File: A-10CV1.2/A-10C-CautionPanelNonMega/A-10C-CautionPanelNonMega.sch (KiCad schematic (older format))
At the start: 29 parts, among them J1 Barrel_Jack, J10 Conn_01x24, J11 Conn_01x24, J13 Conn_01x03, J2 Nano Pins 1-15, J3 Nano Pins 16-30 (reversed), J4 Serial Tx/Rx, J8 Conn_01x24, J9 Conn_01x24, Q1 BC338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

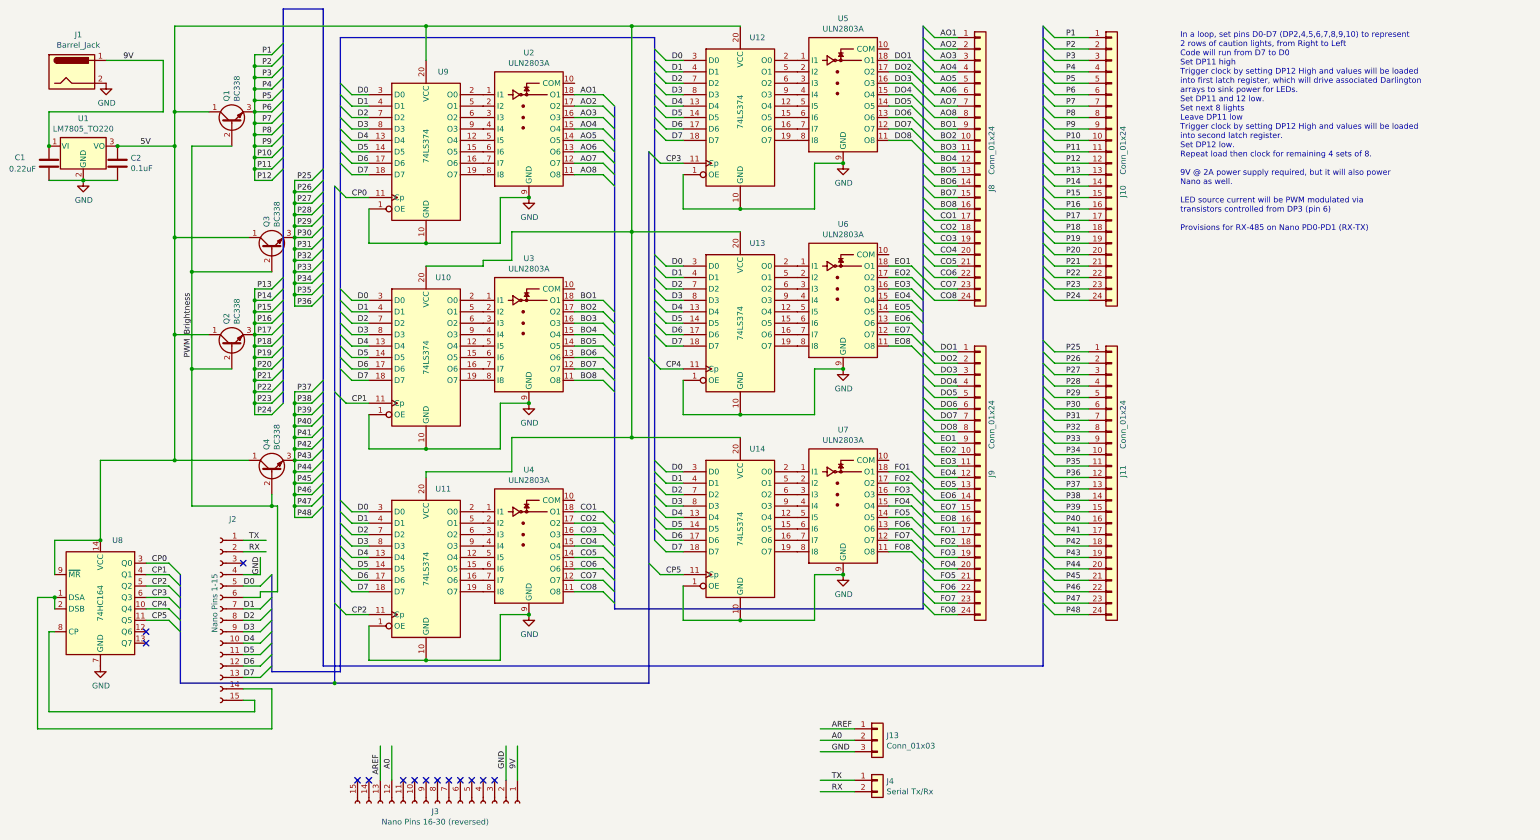
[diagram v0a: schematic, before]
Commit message: First bits of working code completed. May be changed in favor of single event vs 48 events.
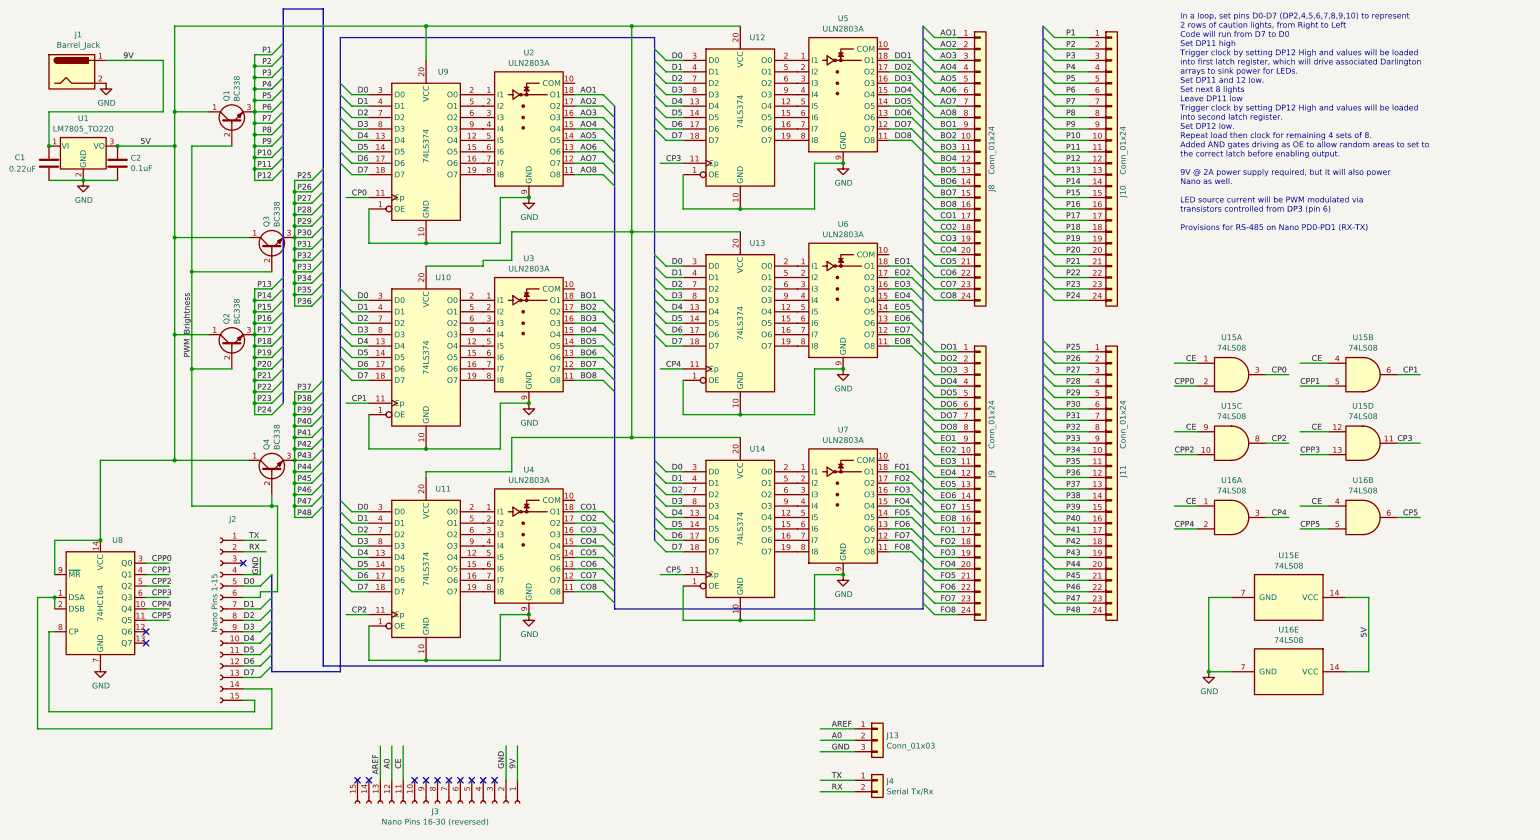
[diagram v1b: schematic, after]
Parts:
- added U15, U16: 74LS08, Package_DIP:DIP-14_W7.62mm, symbol 74xx:74LS08
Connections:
- net labels added: CE, CPP0, CPP1, CPP2, CPP3, CPP4, CPP5
- wire segments 408 -> 433
- no-connect marks 14 -> 13
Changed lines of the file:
@@
 NoConn ~ 1700 6050
 NoConn ~ 1700 6150
-Entry Wire Line
-	1900 5450 2000 5550
-Entry Wire Line
-	1900 5550 2000 5650
-Entry Wire Line
-	1900 5650 2000 5750
-Entry Wire Line
-	1900 5750 2000 5850
-Entry Wire Line
-	1900 5850 2000 5950
-Entry Wire Line
-	1900 5950 2000 6050
 Text Label 1750 5450 0    50   ~ 0
-CP0
+CPP0
 Text Label 1750 5550 0    50   ~ 0
-CP1
+CPP1
 Text Label 1750 5650 0    50   ~ 0
-CP2
+CPP2
 Text Label 1750 5750 0    50   ~ 0
-CP3
+CPP3
 Text Label 1750 5850 0    50   ~ 0
-CP4
+CPP4
 Text Label 1750 5950 0    50   ~ 0
-CP5
+CPP5
 Wire Wire Line
 	3650 5900 3450 5900
-Entry Wire Line
-	3350 5800 3450 5900
 Text Label 3500 5900 0    50   ~ 0
 CP2
 Wire Wire Line
 	3650 2250 3450 2250
-Entry Wire Line
-	3350 2150 3450 2250
 Text Label 3500 2250 0    50   ~ 0
 CP0
 Wire Wire Line
 	3650 4050 3450 4050
-Entry Wire Line
-	3350 3950 3450 4050
 Text Label 3500 4050 0    50   ~ 0
 CP1
 Wire Wire Line
 	6400 1950 6200 1950
-Entry Wire Line
-	6100 1850 6200 1950
 Text Label 6250 1950 0    50   ~ 0
 CP3
 Wire Wire Line
 	6400 3750 6200 3750
-Entry Wire Line
-	6100 3650 6200 3750
 Text Label 6250 3750 0    50   ~ 0
 CP4
 Wire Wire Line
 	6400 5550 6200 5550
-Entry Wire Line
-	6100 5450 6200 5550
 Text Label 6250 5550 0    50   ~ 0
 CP5
-Wire Bus Line
-	2000 6500 3350 6500
-Wire Bus Line
-	3350 6500 6100 6500
-Connection ~ 3350 6500
 Wire Wire Line
 	6400 5650 6400 5950
@@
 NoConn ~ 3550 7350
 NoConn ~ 3650 7350
-NoConn ~ 3950 7350
 NoConn ~ 4050 7350
 NoConn ~ 4150 7350
@@
 NoConn ~ 4750 7350
 Text Notes 10750 2550 0    50   ~ 0
-In a loop, set pins D0-D7 (DP2,4,5,6,7,8,9,10) to represent \n2 rows of caution lights, from Right to Left\nCode will run from D7 to D0\nSet DP11 high\nTrigger clock by setting DP12 High and values will be loaded \ninto first latch register, which will drive associated Darlington\narrays to sink power for LEDs.\nSet DP11 and 12 low.\nSet next 8 lights\nLeave DP11 low\nTrigger clock by setting DP12 High and values will be loaded \ninto second latch register.\nSet DP12 low.\nRepeat load then clock for remaining 4 sets of 8.\n\n9V @ 2A power supply required, but it will also power \nNano as well.\n\nLED source current will be PWM modulated via\ntransistors controlled from DP3 (pin 6)\n\nProvisions for RX-485 on Nano PD0-PD1 (RX-TX)
+In a loop, set pins D0-D7 (DP2,4,5,6,7,8,9,10) to represent \n2 rows of caution lights, from Right to Left\nCode will run from D7 to D0\nSet DP11 high\nTrigger clock by setting DP12 High and values will be loaded \ninto first latch register, which will drive associated Darlington\narrays to sink power for LEDs.\nSet DP11 and 12 low.\nSet next 8 lights\nLeave DP11 low\nTrigger clock by setting DP12 High and values will be loaded \ninto second latch register.\nSet DP12 low.\nRepeat load then clock for remaining 4 sets of 8.\nAdded AND gates driving as OE to allow random areas to set to\nthe correct latch before enabling output.\n\n9V @ 2A power supply required, but it will also power \nNano as well.\n\nLED source current will be PWM modulated via\ntransistors controlled from DP3 (pin 6)\n\nProvisions for RS-485 on Nano PD0-PD1 (RX-TX)
 Wire Wire Line
 	2550 5250 2750 5250
@@
 Wire Wire Line
 	7900 7450 7600 7450
-Wire Bus Line
-	3350 2150 3350 6500
-Wire Bus Line
-	6100 1850 6100 6500
-Wire Bus Line
-	2000 5550 2000 6500
-Wire Bus Line
-	2800 5550 2800 6400
-Wire Bus Line
-	5800 1450 5800 5850
-Wire Bus Line
-	2900 600  2900 4050
-Wire Bus Line
-	3250 600  3250 6350
-Wire Bus Line
-	3400 850  3400 6400
-Wire Bus Line
-	6150 850  6150 5250
-Wire Bus Line
-	8500 750  8500 5850
-Wire Bus Line
-	9550 750  9550 6350
 Text Label 7700 7350 0    50   ~ 0
 TX
 Text Label 7700 7450 0    50   ~ 0
 RX
+$Comp
+L 74xx:74LS08 U15
+U 1 1 5DB94172
+P 11200 3800
+F 0 "U15" H 11200 4125 50  0000 C CNN
+F 1 "74LS08" H 11200 4034 50  0000 C CNN
+F 2 "Package_DIP:DIP-14_W7.62mm" H 11200 3800 50  0001 C CNN
+F 3 "http://www.ti.com/lit/gpn/sn74LS08" H 11200 3800 50  0001 C CNN
+	1    11200 3800
+	1    0    0    -1
+$EndComp
+$Comp
+L 74xx:74LS08 U15
+U 2 1 5DB9F551
+P 12350 3800
+F 0 "U15" H 12350 4125 50  0000 C CNN
+F 1 "74LS08" H 12350 4034 50  0000 C CNN
+F 2 "Package_DIP:DIP-14_W7.62mm" H 12350 3800 50  0001 C CNN
+F 3 "http://www.ti.com/lit/gpn/sn74LS08" H 12350 3800 50  0001 C CNN
+	2    12350 3800
+	1    0    0    -1
+$EndComp
+$Comp
+L 74xx:74LS08 U15
+U 3 1 5DBA130A
+P 11200 4400
+F 0 "U15" H 11200 4725 50  0000 C CNN
+F 1 "74LS08" H 11200 4634 50  0000 C CNN
+F 2 "Package_DIP:DIP-14_W7.62mm" H 11200 4400 50  0001 C CNN
+F 3 "http://www.ti.com/lit/gpn/sn74LS08" H 11200 4400 50  0001 C CNN
+	3    11200 4400
+	1    0    0    -1
+$EndComp
+$Comp
+L 74xx:74LS08 U15
+U 4 1 5DBA2DB5
+P 12350 4400
+F 0 "U15" H 12350 4725 50  0000 C CNN
+F 1 "74LS08" H 12350 4634 50  0000 C CNN
+F 2 "Package_DIP:DIP-14_W7.62mm" H 12350 4400 50  0001 C CNN
+F 3 "http://www.ti.com/lit/gpn/sn74LS08" H 12350 4400 50  0001 C CNN
+	4    12350 4400
+	1    0    0    -1
+$EndComp
+$Comp
+L 74xx:74LS08 U16
+U 1 1 5DBA5072
+P 11200 5050
+F 0 "U16" H 11200 5375 50  0000 C CNN
+F 1 "74LS08" H 11200 5284 50  0000 C CNN
+F 2 "Package_DIP:DIP-14_W7.62mm" H 11200 5050 50  0001 C CNN
+F 3 "http://www.ti.com/lit/gpn/sn74LS08" H 11200 5050 50  0001 C CNN
+	1    11200 5050
+	1    0    0    -1
+$EndComp
+$Comp
+L 74xx:74LS08 U16
+U 2 1 5DBA7423
+P 12350 5050
+F 0 "U16" H 12350 5375 50  0000 C CNN
+F 1 "74LS08" H 12350 5284 50  0000 C CNN
+F 2 "Package_DIP:DIP-14_W7.62mm" H 12350 5050 50  0001 C CNN
+F 3 "http://www.ti.com/lit/gpn/sn74LS08" H 12350 5050 50  0001 C CNN
+	2    12350 5050
+	1    0    0    -1
+$EndComp
+Wire Wire Line
+	10900 3700 10700 3700
+Wire Wire Line
+	10900 3900 10700 3900
+Wire Wire Line
+	10900 4300 10700 4300
+Wire Wire Line
+	10900 4500 10700 4500
+Wire Wire Line
+	10900 4950 10700 4950
+Wire Wire Line
+	10900 5150 10700 5150
+Wire Wire Line
+	12050 3700 11800 3700
+Wire Wire Line
+	12050 3900 11800 3900
+Wire Wire Line
+	12050 4300 11800 4300
+Wire Wire Line
+	12050 4500 11800 4500
+Wire Wire Line
+	12050 4950 11800 4950
+Wire Wire Line
+	12050 5150 11800 5150
+Wire Wire Line
+	11500 3800 11700 3800
+Wire Wire Line
+	11500 4400 11700 4400
+Wire Wire Line
+	11500 5050 11700 5050
+Wire Wire Line
+	12650 3800 12850 3800
+Wire Wire Line
+	12650 4400 12850 4400
+Wire Wire Line
+	12650 5050 12850 5050
+Text Label 11550 3800 0    50   ~ 0
+CP0
+Text Label 12700 3800 0    50   ~ 0
+CP1
+Text Label 11550 4400 0    50   ~ 0
+CP2
+Text Label 12650 4400 0    50   ~ 0
+CP3
+Text Label 11550 5050 0    50   ~ 0
+CP4
+Text Label 12700 5050 0    50   ~ 0
+CP5
+Wire Wire Line
+	3950 7350 3950 7050
+Text Label 3950 7250 1    50   ~ 0
+CE
+Text Label 10800 3700 0    50   ~ 0
+CE
+Text Label 11900 3700 0    50   ~ 0
+CE
+Text Label 10800 4300 0    50   ~ 0
+CE
+Text Label 10800 4950 0    50   ~ 0
+CE
+Text Label 11900 4300 0    50   ~ 0
+CE
+Text Label 11900 4950 0    50   ~ 0
+CE
+Text Label 10700 3900 0    50   ~ 0
+CPP0
+Text Label 11800 3900 0    50   ~ 0
+CPP1
+Text Label 10700 4500 0    50   ~ 0
+CPP2
+Text Label 11800 4500 0    50   ~ 0
+CPP3
+Text Label 10700 5150 0    50   ~ 0
+CPP4
+Text Label 11800 5150 0    50   ~ 0
+CPP5
+$Comp
+L 74xx:74LS08 U15
+U 5 1 5E767546
+P 11700 5750
+F 0 "U15" V 11333 5750 50  0000 C CNN
+F 1 "74LS08" V 11424 5750 50  0000 C CNN
+F 2 "" H 11700 5750 50  0001 C CNN
+F 3 "http://www.ti.com/lit/gpn/sn74LS08" H 11700 5750 50  0001 C CNN
+	5    11700 5750
+	0    1    1    0
+$EndComp
+$Comp
+L 74xx:74LS08 U16
+U 5 1 5E76A619
+P 11700 6400
+F 0 "U16" V 11333 6400 50  0000 C CNN
+F 1 "74LS08" V 11424 6400 50  0000 C CNN
+F 2 "" H 11700 6400 50  0001 C CNN
+F 3 "http://www.ti.com/lit/gpn/sn74LS08" H 11700 6400 50  0001 C CNN
+	5    11700 6400
+	0    1    1    0
+$EndComp
+Wire Wire Line
+	11200 5750 11000 5750
+Wire Wire Line
+	11000 5750 11000 6400
+Wire Wire Line
+	11000 6400 11200 6400
+$Comp
+L power:GND #PWR0101
+U 1 1 5E7B7996
+P 11000 6400
+F 0 "#PWR0101" H 11000 6150 50  0001 C CNN
+F 1 "GND" H 11005 6227 50  0000 C CNN
+F 2 "" H 11000 6400 50  0001 C CNN
+F 3 "" H 11000 6400 50  0001 C CNN
+	1    11000 6400
+	1    0    0    -1
+$EndComp
+Connection ~ 11000 6400
+Wire Wire Line
+	12200 5750 12400 5750
+Wire Wire Line
+	12400 5750 12400 6400
+Wire Wire Line
+	12400 6400 12200 6400
+Text Label 12400 6100 1    50   ~ 0
+5V
+Wire Bus Line
+	2800 5550 2800 6400
+Wire Bus Line
+	5800 1450 5800 5850
+Wire Bus Line
+	2900 600  2900 4050
+Wire Bus Line
+	3250 600  3250 6350
+Wire Bus Line
+	3400 850  3400 6400
+Wire Bus Line
+	6150 850  6150 5250
+Wire Bus Line
+	8500 750  8500 5850
+Wire Bus Line
+	9550 750  9550 6350
 $EndSCHEMATC

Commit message: Correct regulator model
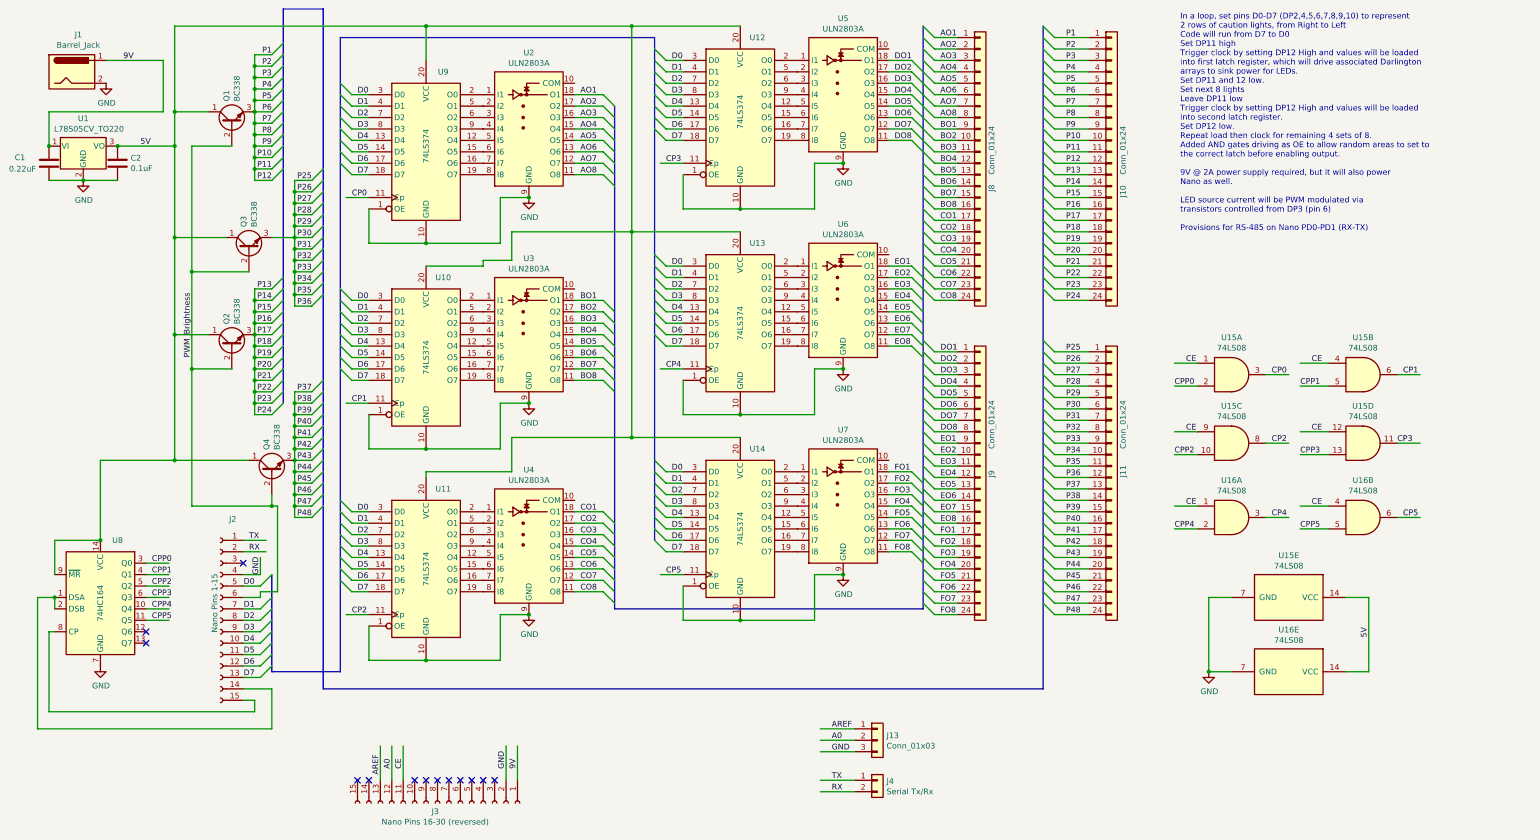
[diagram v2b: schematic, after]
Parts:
- U1: value LM7805_TO220 -> L78S05CV_TO220
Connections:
- wire segments 433 -> 434
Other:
- moved on the sheet: Q3
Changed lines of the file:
@@
 P 1150 1800
 F 0 "U1" H 1150 2042 50  0000 C CNN
-F 1 "LM7805_TO220" H 1150 1951 50  0000 C CNN
+F 1 "L78S05CV_TO220" H 1200 1950 50  0000 C CNN
 F 2 "Package_TO_SOT_THT:TO-220-3_Vertical" H 1150 2025 50  0001 C CIN
 F 3 "http://www.fairchildsemi.com/ds/LM/LM7805.pdf" H 1150 1750 50  0001 C CNN
@@
 L Transistor_BJT:BC338 Q3
 U 1 1 5F354CC3
-P 2800 2700
-F 0 "Q3" H 2991 2746 50  0000 L CNN
-F 1 "BC338" H 2991 2655 50  0000 L CNN
-F 2 "Package_TO_SOT_THT:TO-92_Inline" H 3000 2625 50  0001 L CIN
-F 3 "http://diotec.com/tl_files/diotec/files/pdf/datasheets/bc337" H 2800 2700 50  0001 L CNN
-	1    2800 2700
+P 2600 2700
+F 0 "Q3" H 2791 2746 50  0000 L CNN
+F 1 "BC338" H 2791 2655 50  0000 L CNN
+F 2 "Package_TO_SOT_THT:TO-92_Inline" H 2800 2625 50  0001 L CIN
+F 3 "http://diotec.com/tl_files/diotec/files/pdf/datasheets/bc337" H 2600 2700 50  0001 L CNN
+	1    2600 2700
 	0    -1   -1   0
 $EndComp
@@
 	2450 3750 2100 3750
 Wire Wire Line
-	2100 2900 2800 2900
+	2100 2900 2600 2900
 Wire Wire Line
 	1950 1500 2250 1500
-Wire Wire Line
-	2600 2600 1950 2600
 Wire Wire Line
 	2250 3450 1950 3450
@@
 	2900 600  3250 600
 Wire Bus Line
-	3250 6350 9550 6350
+	3250 6550 9550 6550
 Connection ~ 1950 3450
 Connection ~ 2100 3750
@@
 Text Label 12400 6100 1    50   ~ 0
 5V
+Wire Wire Line
+	2400 2600 1950 2600
+Wire Wire Line
+	2800 2600 3000 2600
 Wire Bus Line
 	2800 5550 2800 6400
@@
 	2900 600  2900 4050
 Wire Bus Line
-	3250 600  3250 6350
+	3250 600  3250 6550
 Wire Bus Line
 	3400 850  3400 6400
@@
 	8500 750  8500 5850
 Wire Bus Line
-	9550 750  9550 6350
+	9550 750  9550 6550
 $EndSCHEMATC

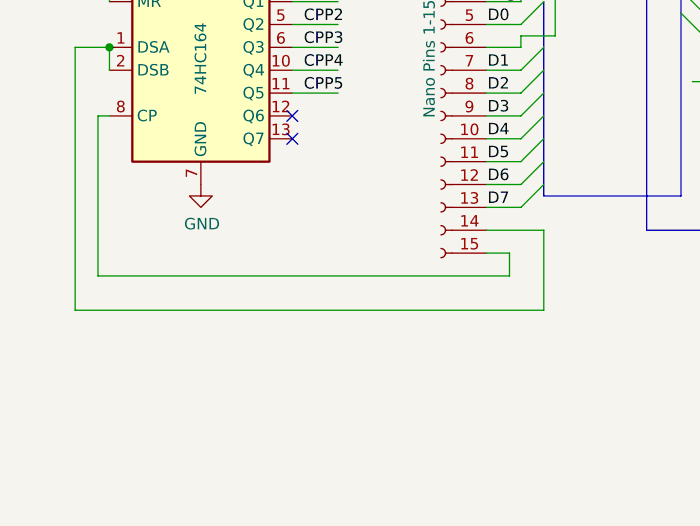
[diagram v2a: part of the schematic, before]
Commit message: Tweaking timing for Nano to 8 bit interface.
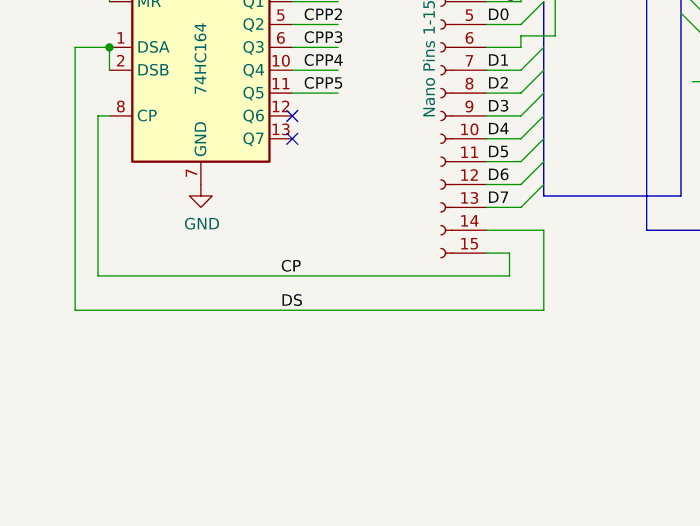
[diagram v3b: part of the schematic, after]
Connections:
- net labels added: CP, DS
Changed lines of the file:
@@
 Wire Bus Line
 	9550 750  9550 6550
+Text Label 1650 6750 0    50   ~ 0
+CP
+Text Label 1650 6900 0    50   ~ 0
+DS
 $EndSCHEMATC
